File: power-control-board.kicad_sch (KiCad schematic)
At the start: 0 parts

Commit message: Basic power handling
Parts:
- added C1, C2: 0.1u, symbol Device:C
- added C3, C4: 10u, symbol Device:C
- added C5, C6: 22u, symbol Device:C
- added J1: Conn_01x02_Socket, symbol Connector:Conn_01x02_Socket
- added J2: Raspberry_Pi_2_3, symbol Connector:Raspberry_Pi_2_3
- added L1: 3.3u, symbol Device:L
- added R1, R2: 10k, symbol Device:R
- added R3: 54.9k, symbol Device:R
- added U1: (no value), symbol Converter_DCDC:TPS565201DDCR
- added U2: XIAO-ESP32-C6-DIP, symbol Microcontrollers:XIAO-ESP32-C6-DIP
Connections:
- new net: J2.1 (3V3), J2.17 (3V3)
- new net: J2.14 (GND), J2.20 (GND), J2.25 (GND), J2.30 (GND), J2.34 (GND), J2.39 (GND), J2.6 (GND), J2.9 (GND)
- new net: J2.2 (5V), J2.4 (5V)
- new net: R1.1, U1.5 (EN)
- new net: C1.1, L1.2, U1.2 (SW)
- new net: R2.1, R3.2, U1.4 (VFB)
- new net: C1.2, U1.6 (VBST)
- new net +5V: R3.1
- new net BC12T5EN: R1.2
- new net GND: C2.1, C3.1, C4.1, C5.2, C6.2, J1.2 (Pin_2), R2.2, U1.1 (GND), U1.3 (VIN)
- new net VIN: C2.2, C3.2, C4.2, J1.1 (Pin_1)
- new net VOUT: C5.1, C6.1, L1.1
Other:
- note added: "Buck Converter (12V-5V)"
- note added: "Connectors"
- note added: "TPS565201DDCR (Buck Converter)"

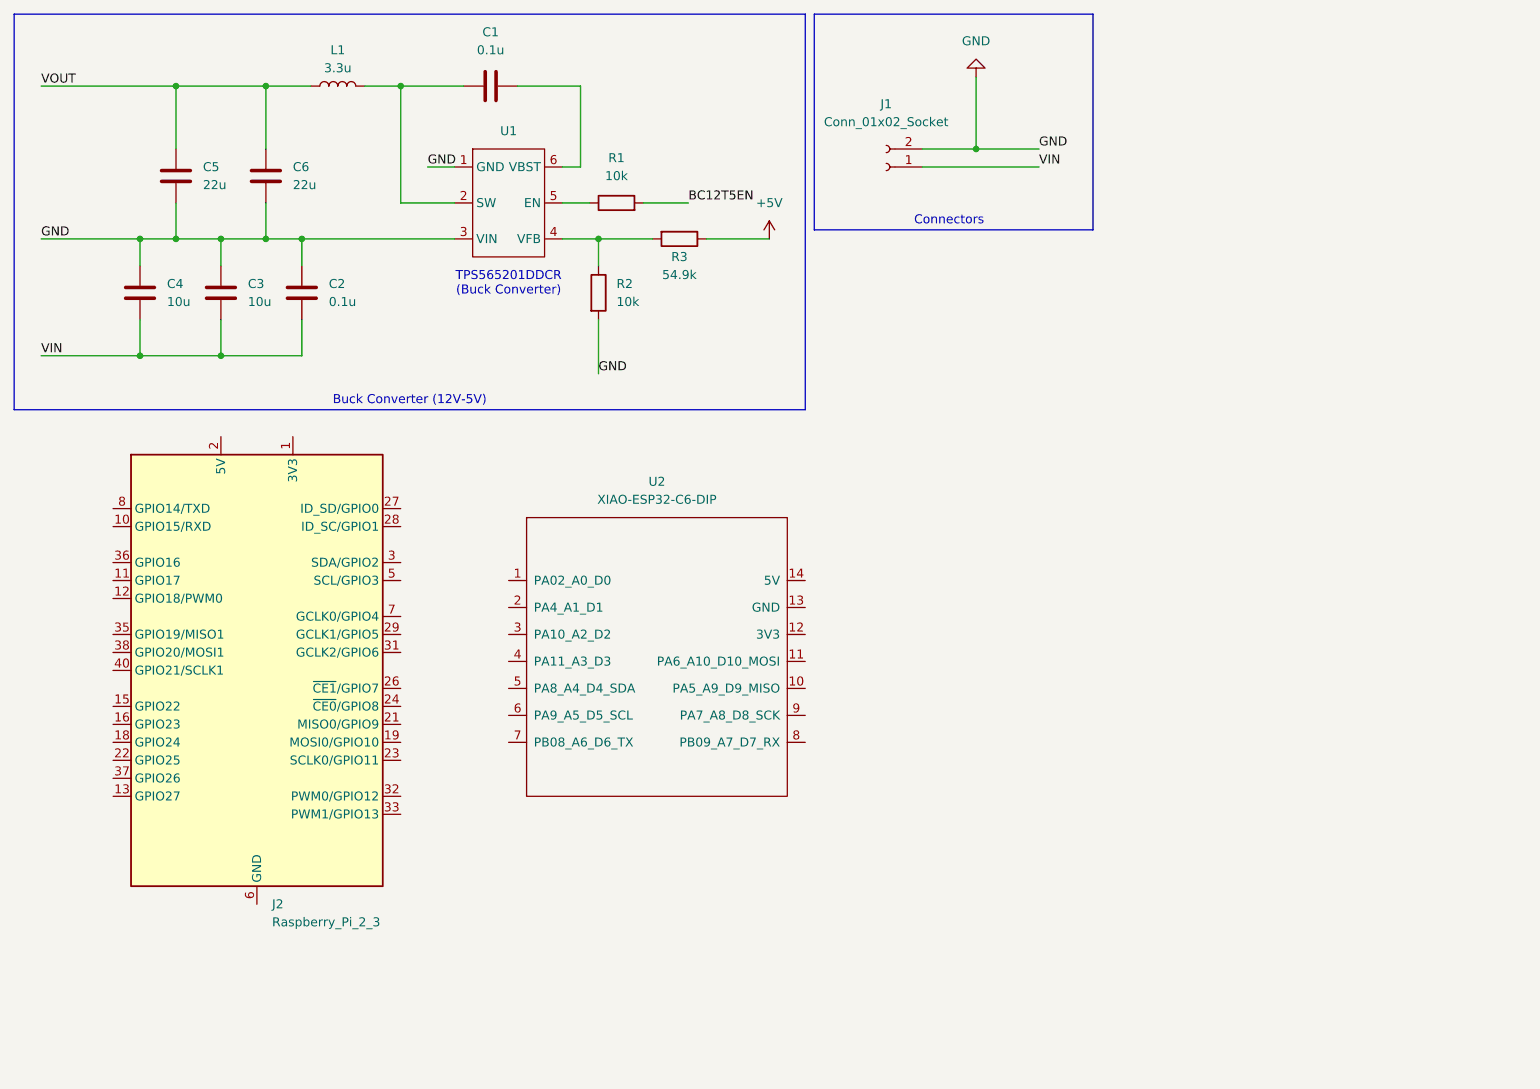
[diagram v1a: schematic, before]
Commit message: Added microcontrollers, thermal module, and several temp sensors, no current protection circuitry etc
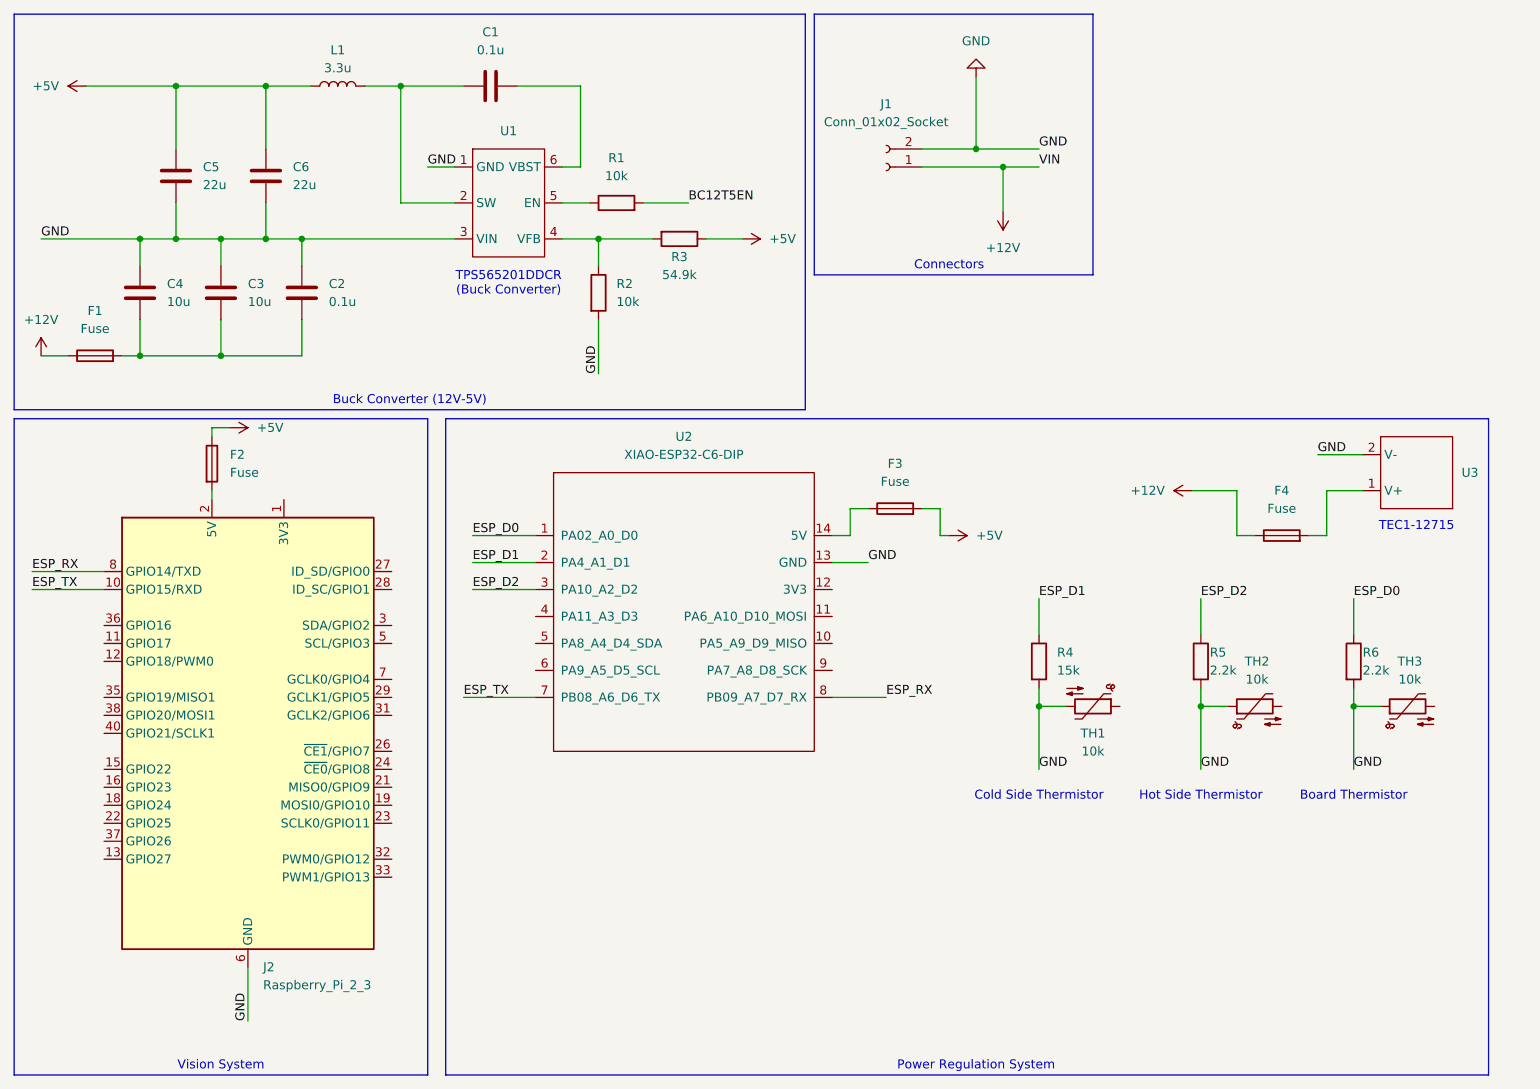
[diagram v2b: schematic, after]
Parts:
- added F1, F2, F3, F4: Fuse, symbol Device:Fuse
- added R4: 15k, symbol Device:R
- added R5, R6: 2.2k, symbol Device:R
- added TH1, TH2, TH3: 10k, symbol Device:Thermistor_NTC
- added U3: (no value), symbol Misc_Parts:TEC1-12715
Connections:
- net VOUT is gone; now on net +5V: C5.1, C6.1, L1.1
- net +5V: now also F2.1, F3.2
- net GND: now also J2.14 (GND), J2.20 (GND), J2.25 (GND), J2.30 (GND), J2.34 (GND), J2.39 (GND), J2.6 (GND), J2.9 (GND), U2.13 (GND), R4.2, R5.2, R6.2, TH1.2, TH2.1, TH3.1, U3.2 (V-)
- net ESP_TX: now reaches J2.10 (GPIO15/RXD)
- net ESP_TX: now also U2.7 (PB08_A6_D6_TX)
- net at J2.2 (5V), J2.4 (5V): now also F2.2
- net ESP_RX: now reaches J2.8 (GPIO14/TXD)
- net ESP_RX: now also U2.8 (PB09_A7_D7_RX)
- net ESP_D0: now reaches U2.1 (PA02_A0_D0)
- net ESP_D0: now also R6.1
- net at U2.14 (5V): now also F3.1
- net ESP_D1: now reaches U2.2 (PA4_A1_D1)
- net ESP_D1: now also R4.1
- net ESP_D2: now reaches U2.3 (PA10_A2_D2)
- net ESP_D2: now also R5.1
- net VIN: no longer names the net of C2.2, C3.2, C4.2
- net VIN: now also F1.2; no longer J1.1 (Pin_1)
- new net: F4.2, U3.1 (V+)
- new net +12V: F1.1, F4.1, J1.1 (Pin_1)
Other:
- note added: "Board Thermistor"
- note added: "Cold Side Thermistor"
- note added: "Hot Side Thermistor"
- note added: "Power Regulation System"
- note added: "TEC1-12715"
- note added: "Vision System"
- moved on the sheet: J2, U2

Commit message: Fix thermistor layout
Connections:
- net ESP_D0: now also TH3.2; no longer R6.1
- net ESP_D1: now also TH1.1; no longer R4.1
- net ESP_D2: now also TH2.2; no longer R5.1
- net ESP_3V3: now reaches U2.12 (3V3)
- net ESP_3V3: now also R4.1, R5.1, R6.1
- no-connect marks 0 -> 33
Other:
- moved on the sheet: R4, R5, R6, TH1, TH2, TH3

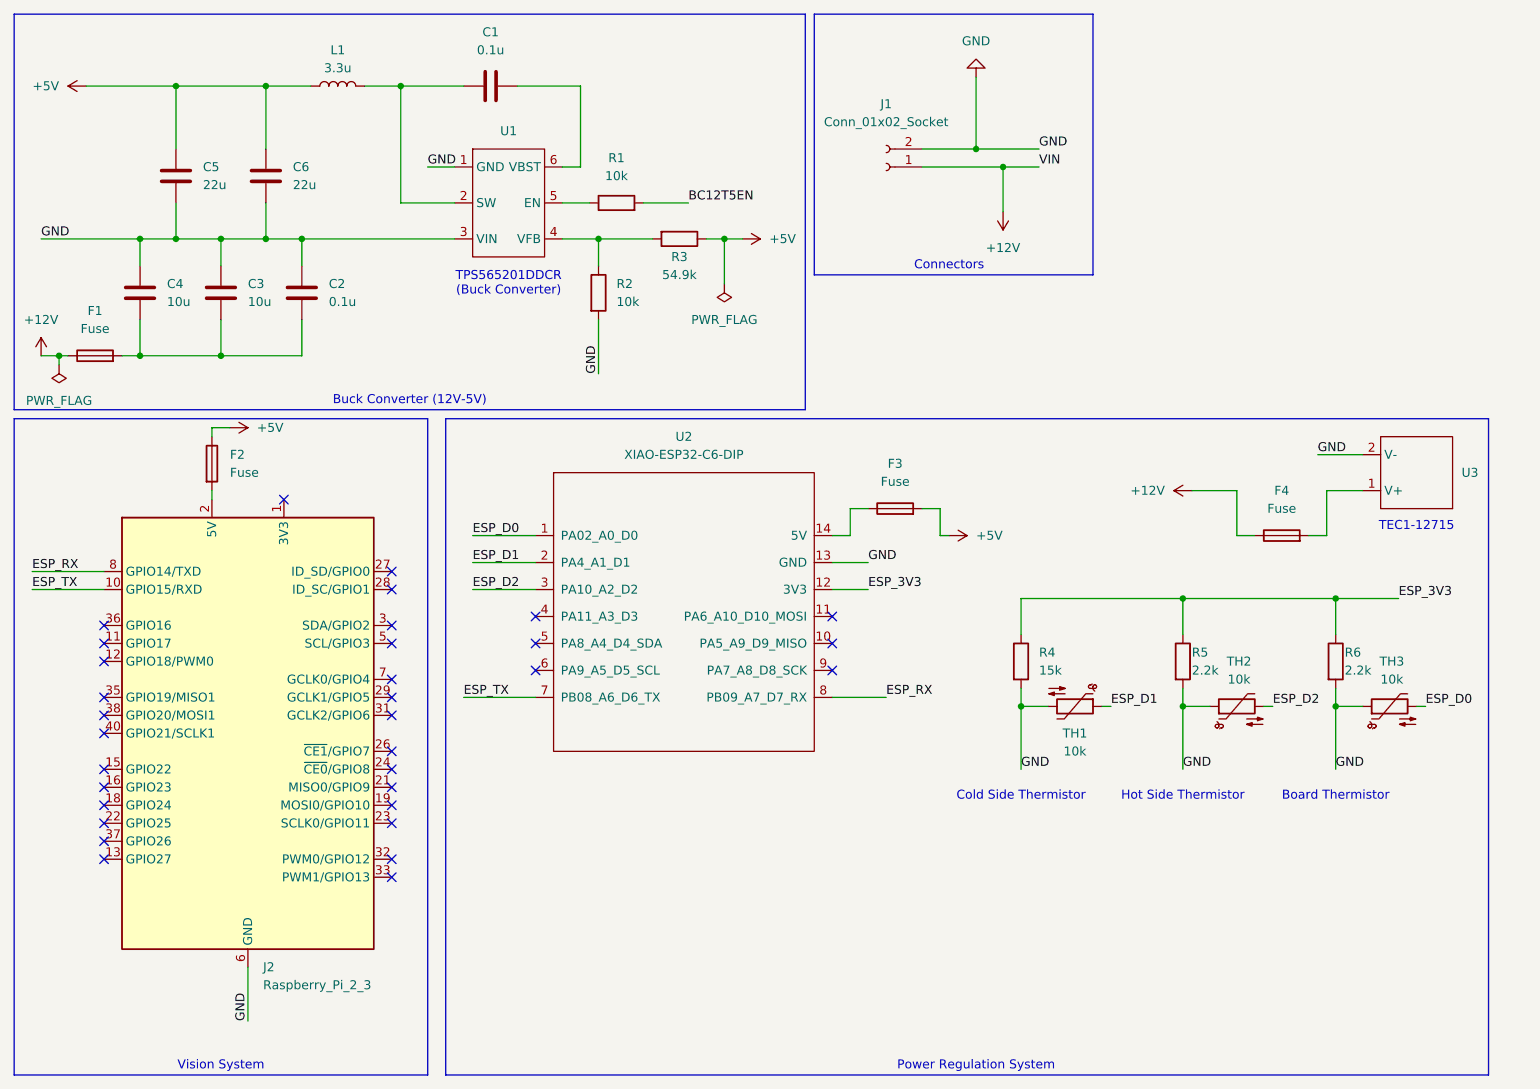
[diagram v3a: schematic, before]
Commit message: Fixed some ERC errors
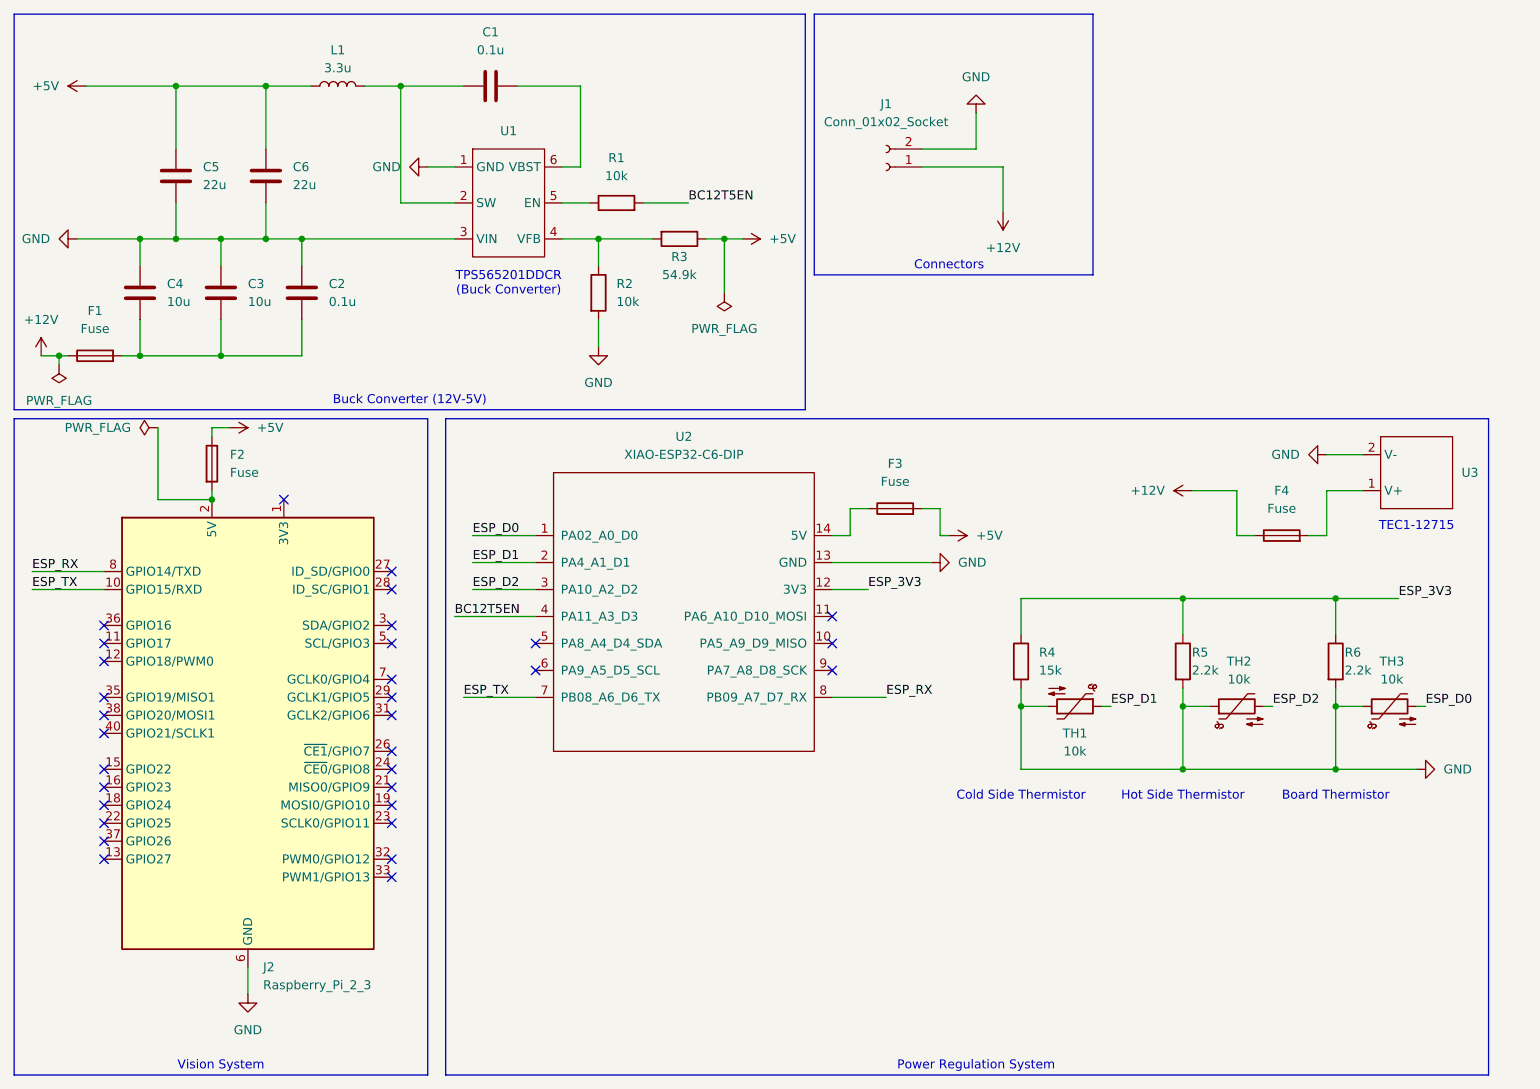
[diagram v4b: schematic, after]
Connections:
- net BC12T5EN: now also U2.4 (PA11_A3_D3)
- no-connect marks 33 -> 32
